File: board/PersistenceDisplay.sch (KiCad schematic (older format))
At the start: 34 parts, among them J1 Conn_01x01, J2 Conn_01x01, J5 Conn_01x01, J6 Conn_01x01, J8 Conn_01x01, J9 Conn_01x01, U4 LM393

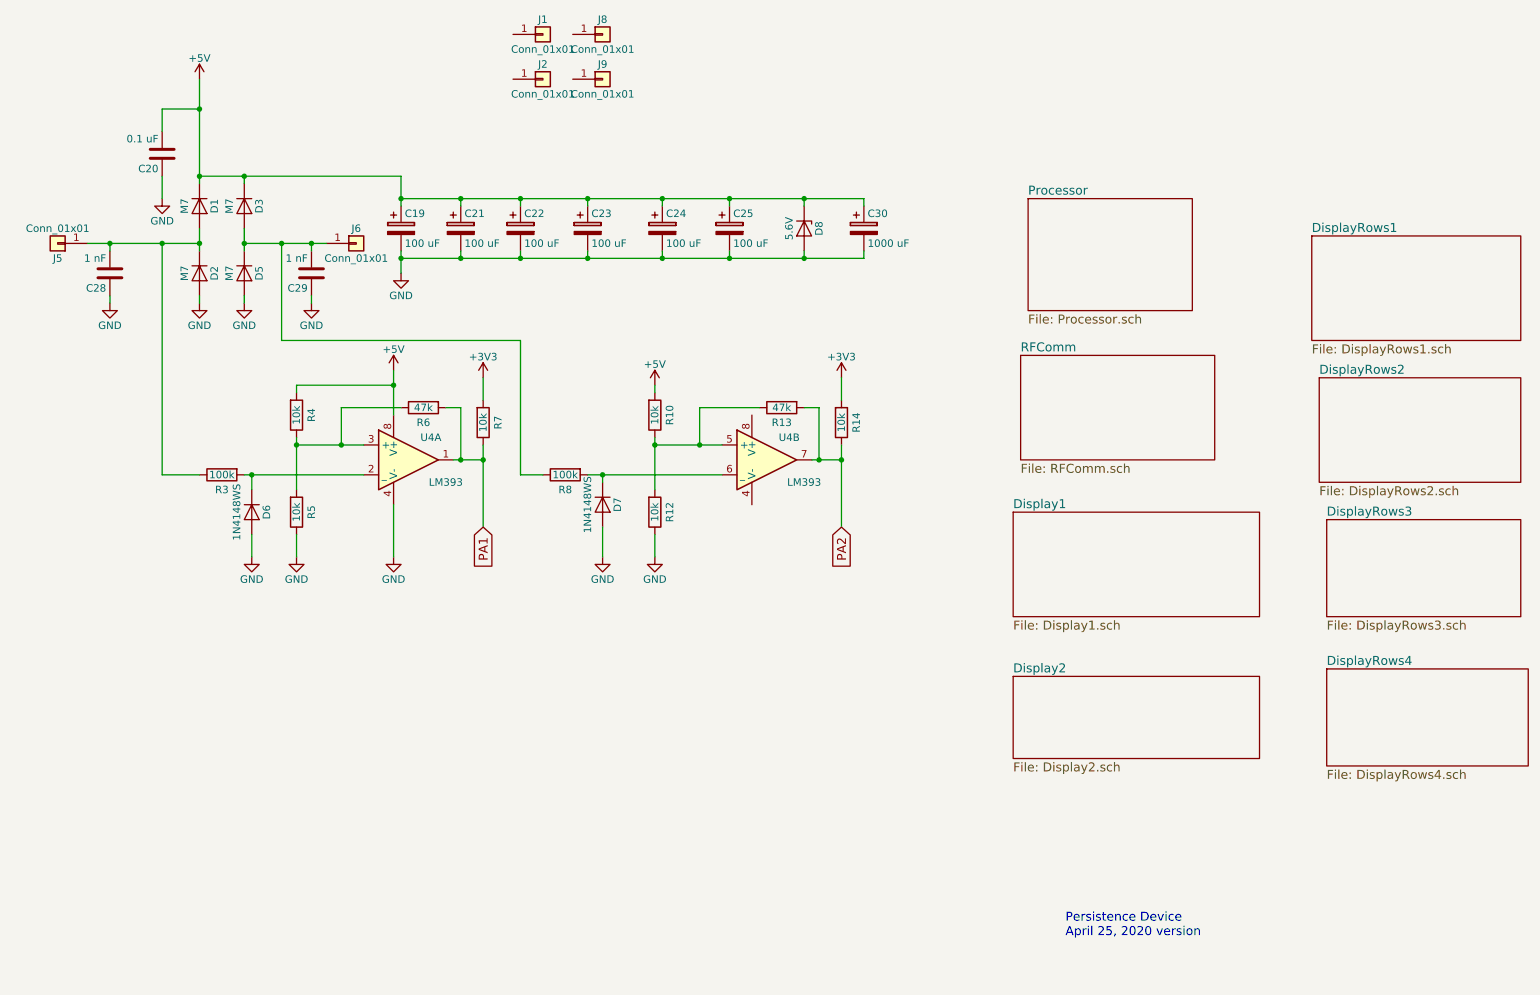
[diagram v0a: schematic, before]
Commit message: Moved around components and added cutouts
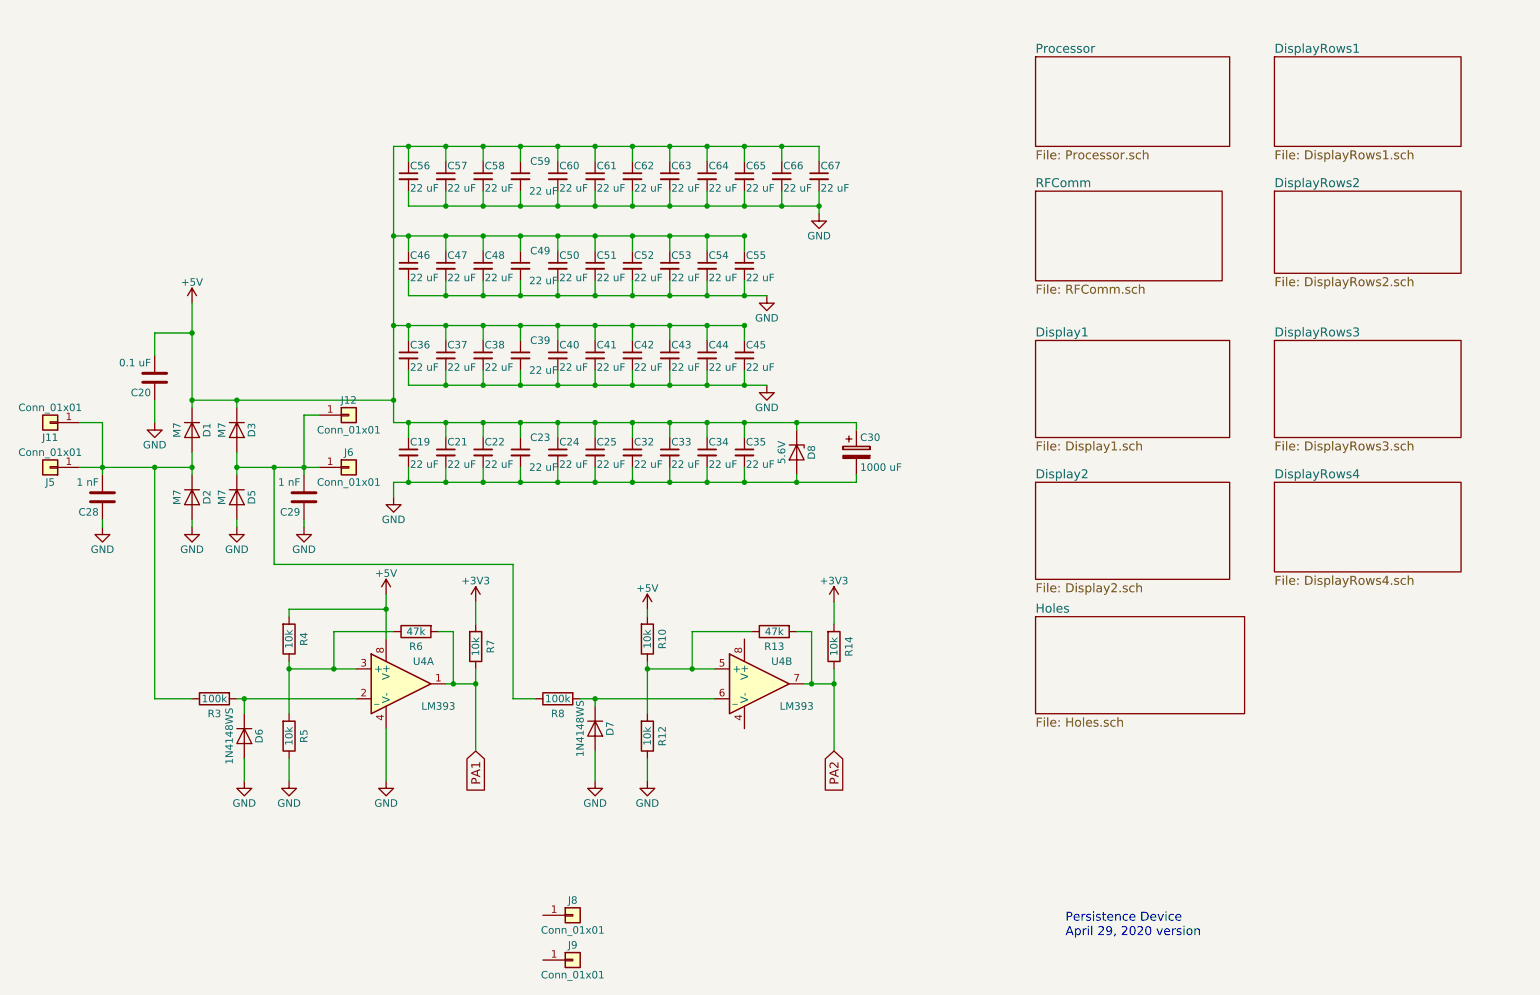
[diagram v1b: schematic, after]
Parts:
- removed C19, C21, C22, C23, C24, C25: 100 uF, Capacitors_SMD:C_1210_HandSoldering, symbol CP
- removed J1, J2: Conn_01x01, PersistenceDisplay:BigSlot, symbol Conn_01x01
- added C19, C21, C22, C23, C24, C25, C32, C33, C34, C35, C36, C37, C38, C39, C40, C41, C42, C43, C44, C45, C46, C47, C48, C49, C50, C51, C52, C53, C54, C55, C56, C57, C58, C59, C60, C61, C62, C63, C64, C65, C66, C67: 22 uF, Capacitors_SMD:C_0603, symbol C_Small
- added J11, J12: Conn_01x01, PersistenceDisplay:ContactPad, symbol Conn_01x01
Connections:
- net +5V: now also C19.1, C21.1, C22.1, C23.1, C24.1, C25.1, C32.1, C33.1, C34.1, C35.1, C36.1, C37.1, C38.1, C39.1, C40.1, C41.1, C42.1, C43.1, C44.1, C45.1, C46.1, C47.1, C48.1, C49.1, C50.1, C51.1, C52.1, C53.1, C54.1, C55.1, C56.1, C57.1, C58.1, C59.1, C60.1, C61.1, C62.1, C63.1, C64.1, C65.1, C66.1, C67.1
- net GND: now also C19.2, C21.2, C22.2, C23.2, C24.2, C25.2, C32.2, C33.2, C34.2, C35.2, C36.2, C37.2, C38.2, C39.2, C40.2, C41.2, C42.2, C43.2, C44.2, C45.2, C46.2, C47.2, C48.2, C49.2, C50.2, C51.2, C52.2, C53.2, C54.2, C55.2, C56.2, C57.2, C58.2, C59.2, C60.2, C61.2, C62.2, C63.2, C64.2, C65.2, C66.2, C67.2
- net at C28.2, D1.2 (A), D2.1 (K)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: now also J11.1 (Pin_1)
- net at C29.2, D3.2 (A), D5.1 (K)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: now also J12.1 (Pin_1)
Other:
- note added: "Persistence Device\nApril 29, 2020 version"
- note removed: "Persistence Device\nApril 25, 2020 version"
- moved on the sheet: C20, C28, C29, C30, D1, D2, D3, D5, D6, D7, D8, J5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

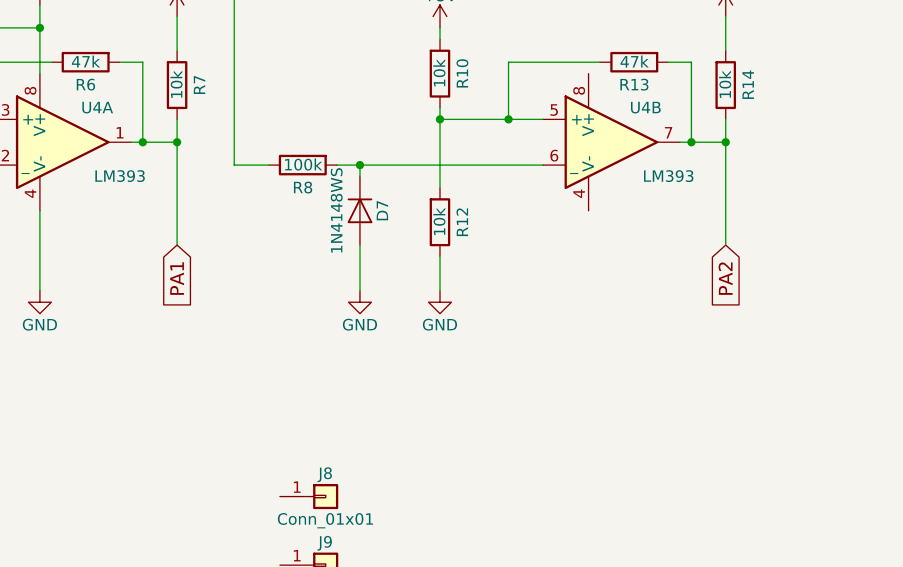
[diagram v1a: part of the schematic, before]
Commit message: Moved the brushes to the other side of the board
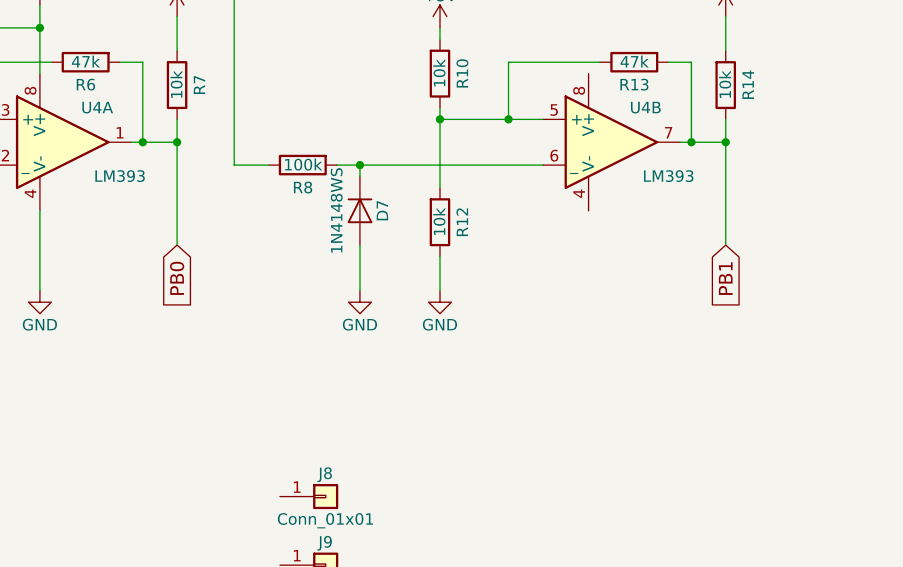
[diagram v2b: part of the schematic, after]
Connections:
- net PA1 renamed PB0
- net PA2 renamed PB1
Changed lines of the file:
@@
 $EndComp
 Text GLabel 3600 5700 3    60   Input ~ 0
-PA1
+PB0
 $Comp
 L GND #PWR2
@@
 $EndComp
 Text GLabel 6000 5700 3    60   Input ~ 0
-PA2
+PB1
 $Comp
 L LM393 U4

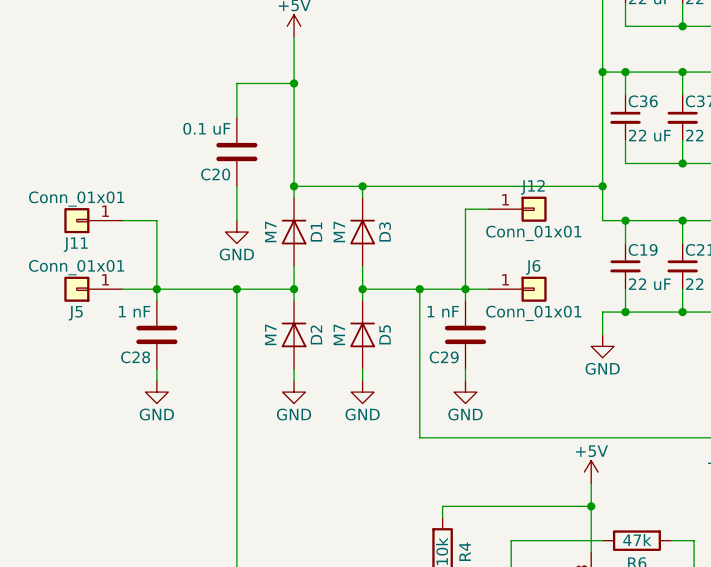
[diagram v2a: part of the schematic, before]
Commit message: Added board holder FreeCAD file
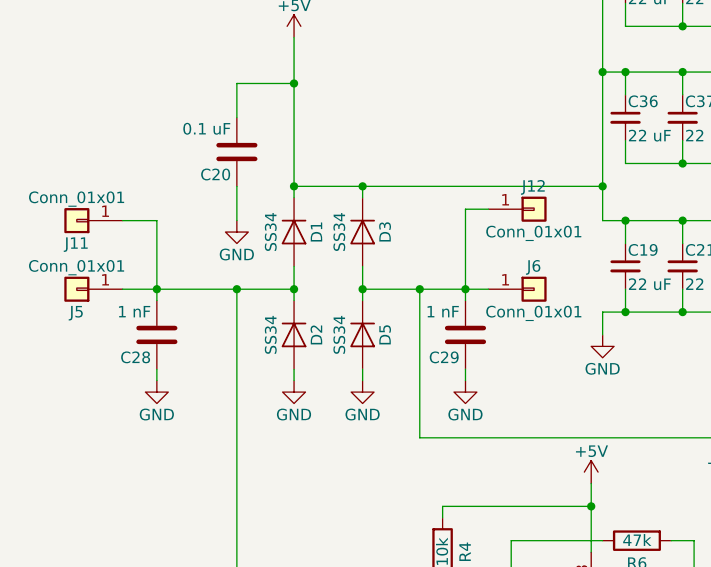
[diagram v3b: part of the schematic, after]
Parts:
- D1, D2, D3, D5: value M7 -> SS34; LCSC C95872 -> C8678
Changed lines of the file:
@@
 P 1700 3550
 F 0 "D1" H 1700 3650 50  0000 C CNN
-F 1 "M7" H 1700 3450 50  0000 C CNN
+F 1 "SS34" H 1700 3450 50  0000 C CNN
 F 2 "Diodes_SMD:D_SMA" H 1700 3550 50  0001 C CNN
 F 3 "" H 1700 3550 50  0001 C CNN
-F 4 "C95872" H 1700 3550 60  0001 C CNN "LCSC"
+F 4 "C8678" H 1700 3550 60  0001 C CNN "LCSC"
 	1    1700 3550
 	0    1    1    0
@@
 P 1700 4000
 F 0 "D2" H 1700 4100 50  0000 C CNN
-F 1 "M7" H 1700 3900 50  0000 C CNN
+F 1 "SS34" H 1700 3900 50  0000 C CNN
 F 2 "Diodes_SMD:D_SMA" H 1700 4000 50  0001 C CNN
 F 3 "" H 1700 4000 50  0001 C CNN
-F 4 "C95872" H 1700 4000 60  0001 C CNN "LCSC"
+F 4 "C8678" H 1700 4000 60  0001 C CNN "LCSC"
 	1    1700 4000
 	0    1    1    0
@@
 P 2000 4000
 F 0 "D5" H 2000 4100 50  0000 C CNN
-F 1 "M7" H 2000 3900 50  0000 C CNN
+F 1 "SS34" H 2000 3900 50  0000 C CNN
 F 2 "Diodes_SMD:D_SMA" H 2000 4000 50  0001 C CNN
 F 3 "" H 2000 4000 50  0001 C CNN
-F 4 "C95872" H 2000 4000 60  0001 C CNN "LCSC"
+F 4 "C8678" H 2000 4000 60  0001 C CNN "LCSC"
 	1    2000 4000
 	0    1    1    0
@@
 P 2000 3550
 F 0 "D3" H 2000 3650 50  0000 C CNN
-F 1 "M7" H 2000 3450 50  0000 C CNN
+F 1 "SS34" H 2000 3450 50  0000 C CNN
 F 2 "Diodes_SMD:D_SMA" H 2000 3550 50  0001 C CNN
 F 3 "" H 2000 3550 50  0001 C CNN
-F 4 "C95872" H 2000 3550 60  0001 C CNN "LCSC"
+F 4 "C8678" H 2000 3550 60  0001 C CNN "LCSC"
 	1    2000 3550
 	0    1    1    0

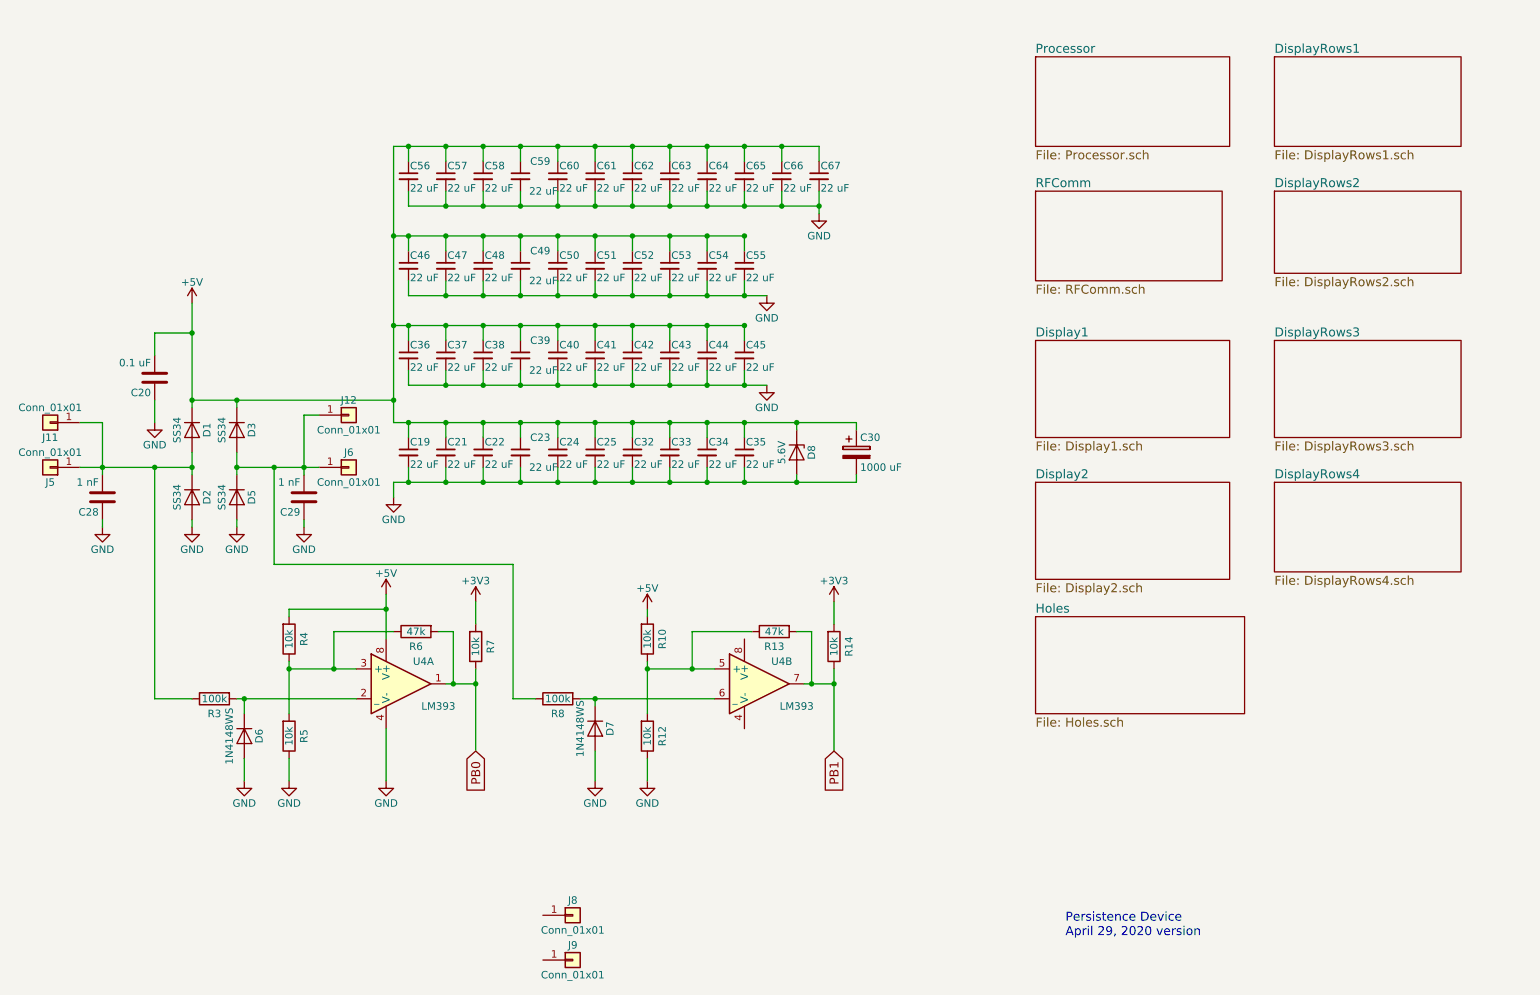
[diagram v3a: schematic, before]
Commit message: Changed to using hall effect sensors
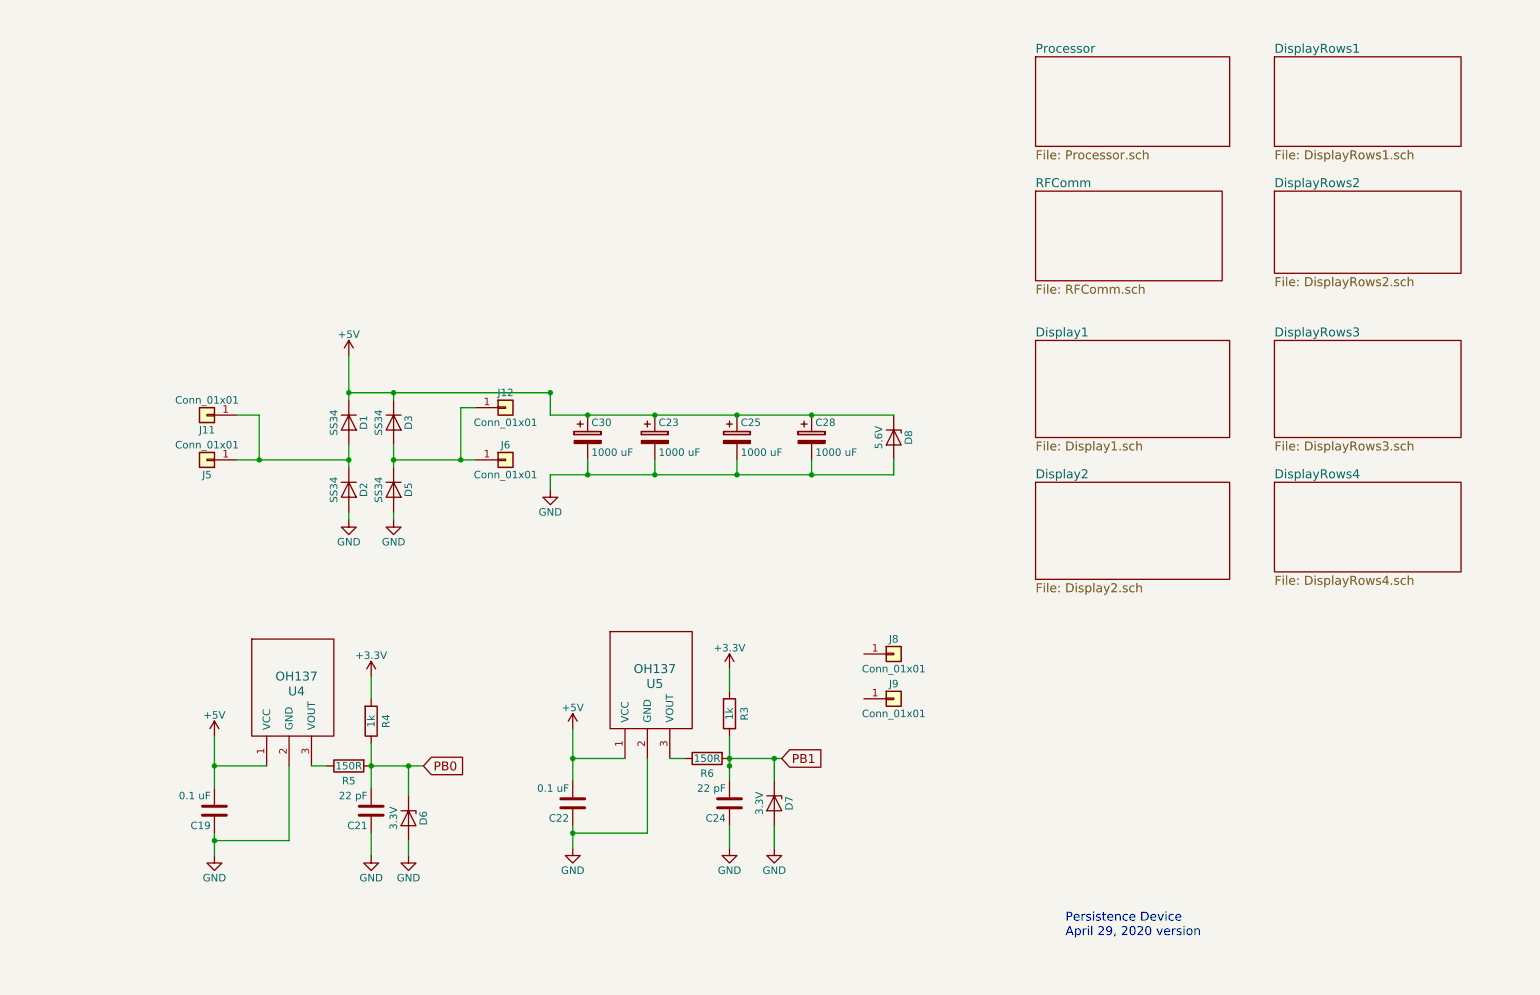
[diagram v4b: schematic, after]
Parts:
- removed C19, C21, C22, C23, C24, C25, C32, C33, C34, C35, C36, C37, C38, C39, C40, C41, C42, C43, C44, C45, C46, C47, C48, C49, C50, C51, C52, C53, C54, C55, C56, C57, C58, C59, C60, C61, C62, C63, C64, C65, C66, C67: 22 uF, Capacitors_SMD:C_0603, symbol C_Small
- removed C20: 0.1 uF, Capacitors_SMD:C_0805_HandSoldering, symbol C
- removed C28, C29: 1 nF, Capacitors_SMD:C_0805_HandSoldering, symbol C
- removed D6, D7: 1N4148WS, Diodes_SMD:D_SOD-323_HandSoldering, symbol D
- removed R10, R12, R14, R7: 10k, Resistors_SMD:R_0805_HandSoldering, symbol R
- removed R13: 47k, Resistors_SMD:R_0805_HandSoldering, symbol R
- removed R8: 100k, Resistors_SMD:R_0805_HandSoldering, symbol R
- removed U4: LM393, Housings_SOIC:SOIC-8_3.9x4.9mm_Pitch1.27mm, symbol LM393
- added C19, C22: 0.1 uF, Capacitors_SMD:C_0805_HandSoldering, symbol C
- added C21, C24: 22 pF, Capacitors_SMD:C_0805_HandSoldering, symbol C
- added C23, C25, C28: 1000 uF, Capacitors_SMD:CP_Elec_10x10.5, symbol CP
- added D6, D7: 3.3V, Diodes_SMD:D_MiniMELF, symbol D_Zener
- added U4, U5: OH137, TO_SOT_Packages_THT:TO-92_Inline_Wide, symbol OH137
- R3: value 100k -> 1k; LCSC C17407 -> C17513
- R4: value 10k -> 1k; LCSC C17414 -> C17513
- R5: value 10k -> 150R; LCSC C17414 -> C17471
- R6: value 47k -> 150R; LCSC C17713 -> C17471
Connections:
- net +3V3: now also R3.2, R4.2
- net +5V: now also C19.2, C22.2, C23.1, C25.1, C28.1, U4.1 (VCC), U5.1 (VCC); no longer R4.2
- net GND: now also C19.1, C21.1, C22.1, C23.2, C24.1, C25.2, C28.2, D6.2 (A), D7.2 (A), U4.2 (GND), U5.2 (GND); no longer R5.1
- net PB0: now also R4.1, R5.2, C21.2, D6.1 (K); no longer R6.2
- net PB1: now also R3.1, R6.2, C24.2, D7.1 (K)
- net at D1.2 (A), D2.1 (K), J11.1 (Pin_1)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: no longer R3.1
- new net: R5.1, U4.3 (VOUT)
- new net: R6.1, U5.3 (VOUT)
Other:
- moved on the sheet: C30, D1, D2, D3, D5, D8, J11, J12, J5, J6, J8, J9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
